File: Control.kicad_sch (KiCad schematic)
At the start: 19 parts, among them U301 ESP32-C3-WROOM-02, U302 MCP100-270D

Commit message: add git hash
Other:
- title: (none) -> ZM108x, Z57x nixieboard
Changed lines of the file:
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@@
 (kicad_sch (version 20230121) (generator eeschema)
   (paper "A4")
+  (title_block
+    (title "ZM108x, Z57x nixieboard")
+    (date "2025-09-04")
+    (rev "3/${GITHASH}")
+    (comment 1 "Atuthor: Martin Sabol")
+  )
   (junction (at 119.38 95.25) (diameter 0) (color 0 0 0 0)
   )

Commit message: schema: bom: PNs update
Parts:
- C301, C302: SPN CL10B105KO8NNNC -> CL21B105KOFNNNE
- C303: SPN CL10B105KO8NNNC -> CL21B104KBCNNNC
- R301, R302, R303: SPN RC0603FR-073K3 -> 0805S8F1002T5E
- U301: SPN (none) -> ESP32-C3-WROOM-02-H4
- U302: SPN (none) -> MCP100T-270I/TT
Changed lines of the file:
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@@
       (effects (font (size 1.27 1.27)) hide)
     )
-    (property "SPN" "RC0603FR-073K3" (at 208.28 64.77 0)
+    (property "SPN" "0805S8F1002T5E" (at 208.28 64.77 0)
       (effects (font (size 1.27 1.27)) hide)
     )
@@
       (effects (font (size 1.27 1.27)) hide)
     )
-    (property "SPN" "CL10B105KO8NNNC" (at 251.46 92.71 0)
+    (property "SPN" "CL21B105KOFNNNE" (at 251.46 92.71 0)
       (effects (font (size 1.27 1.27)) hide)
     )
@@
       (effects (font (size 1.27 1.27)) hide)
     )
+    (property "SPN" "MCP100T-270I/TT" (at 226.06 72.39 0)
+      (effects (font (size 1.27 1.27)) hide)
+    )
     (pin "2")
     (pin "3")
@@
       (effects (font (size 1.27 1.27)) hide)
     )
-    (property "SPN" "CL10B105KO8NNNC" (at 260.35 92.71 0)
+    (property "SPN" "CL21B104KBCNNNC" (at 260.35 92.71 0)
       (effects (font (size 1.27 1.27)) hide)
     )
@@
       (effects (font (size 1.27 1.27)) hide)
     )
-    (property "SPN" "CL10B105KO8NNNC" (at 208.28 96.52 0)
+    (property "SPN" "CL21B105KOFNNNE" (at 208.28 96.52 0)
       (effects (font (size 1.27 1.27)) hide)
     )
@@
       (effects (font (size 1.27 1.27)) hide)
     )
-    (property "SPN" "RC0603FR-073K3" (at 114.3 73.66 0)
+    (property "SPN" "0805S8F1002T5E" (at 114.3 73.66 0)
       (effects (font (size 1.27 1.27)) hide)
     )
@@
     )
     (property "Datasheet" "https://www.espressif.com/sites/default/files/documentation/esp32-c3-wroom-02_datasheet_en.pdf" (at 154.94 130.81 0)
+      (effects (font (size 1.27 1.27)) hide)
+    )
+    (property "SPN" "ESP32-C3-WROOM-02-H4" (at 152.4 97.79 0)
       (effects (font (size 1.27 1.27)) hide)
     )
@@
       (effects (font (size 1.27 1.27)) hide)
     )
-    (property "SPN" "RC0603FR-073K3" (at 119.38 73.66 0)
-      (effects (font (size 1.27 1.27)) hide)
-    )
+    (property "SPN" "0805S8F1002T5E" (at 119.38 73.66 0)
+      (effects (font (size 1.27 1.27)) hide)
+    )

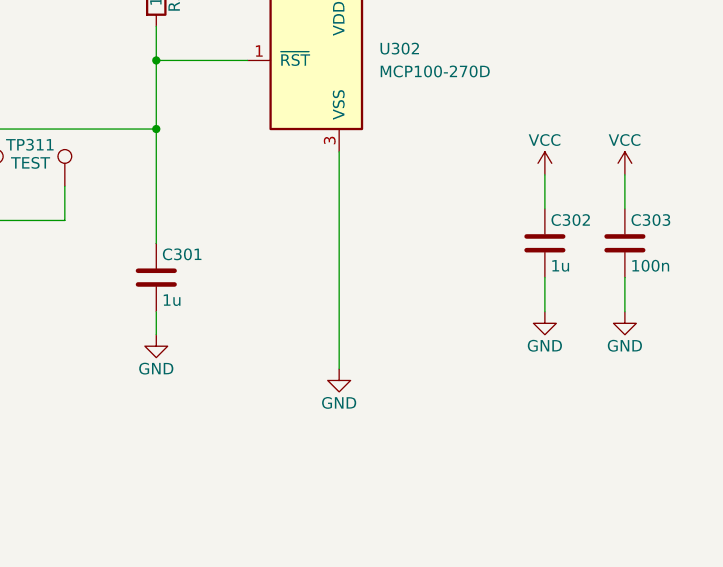
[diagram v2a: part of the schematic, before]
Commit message: BoM: optimize parts
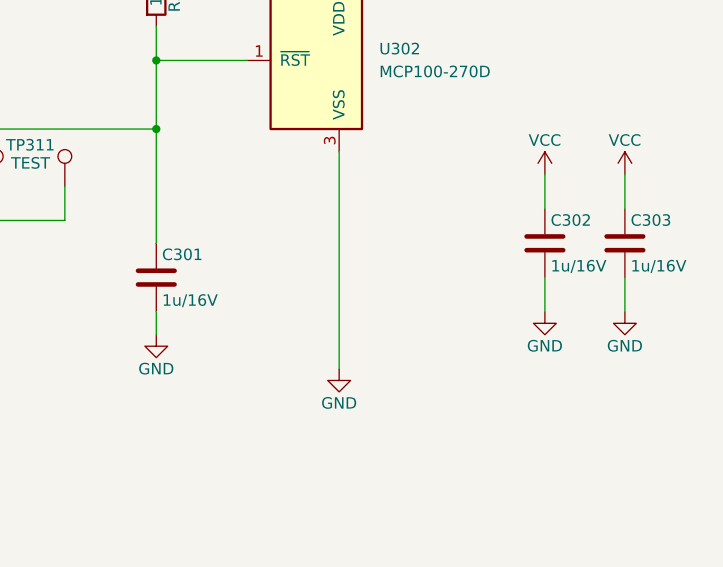
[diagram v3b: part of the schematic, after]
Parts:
- C301, C302: value 1u -> 1u/16V
- C303: value 100n -> 1u/16V; SPN CL21B104KBCNNNC -> CL21B105KOFNNNE
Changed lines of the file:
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@@
       (effects (font (size 1.27 1.27)) (justify left))
     )
-    (property "Value" "1u" (at 252.095 95.25 0)
+    (property "Value" "1u/16V" (at 252.095 95.25 0)
       (effects (font (size 1.27 1.27)) (justify left))
     )
@@
       (effects (font (size 1.27 1.27)) (justify left))
     )
-    (property "Value" "100n" (at 260.985 95.25 0)
+    (property "Value" "1u/16V" (at 260.985 95.25 0)
       (effects (font (size 1.27 1.27)) (justify left))
     )
@@
       (effects (font (size 1.27 1.27)) hide)
     )
-    (property "SPN" "CL21B104KBCNNNC" (at 260.35 92.71 0)
+    (property "SPN" "CL21B105KOFNNNE" (at 260.35 92.71 0)
       (effects (font (size 1.27 1.27)) hide)
     )
@@
       (effects (font (size 1.27 1.27)) (justify left))
     )
-    (property "Value" "1u" (at 208.915 99.06 0)
-      (effects (font (size 1.27 1.27)) (justify left))
-    )
+    (property "Value" "1u/16V" (at 208.915 99.06 0)
+      (effects (font (size 1.27 1.27)) (justify left))
+    )
